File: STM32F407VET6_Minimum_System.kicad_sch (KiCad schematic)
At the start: 29 parts, among them J2 Conn_01x05, J4 Barrel_Jack, Q1 AO3401A, SW2 SW_DIP_x01, U1 STM32F407VET, U2 AMS1117-3.3, Y1 8MHz

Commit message: fix: adjust the wiring label
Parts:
- removed J2: Conn_01x05, symbol Connector_Generic:Conn_01x05
- renumbered C13 to C1, C8 to C10, C15 to C11, C9 to C12, C10 to C13, C16 to C14, C5 to C15, C11 to C16, C12 to C17, C20-bulk to C18, C14 to C2, C20 to C3, C1 to C4, C2 to C5, C19 to C6, C6 to C7, C4 to C8, C7 to C9, F2 to F1, J4 to J1, R6 to R2, SW2 to SW1
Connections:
- net +3.3V: now also C6.2, U1.6 (VBAT); no longer C6.1
- net GND: now also C6.1
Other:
- moved on the sheet: C6

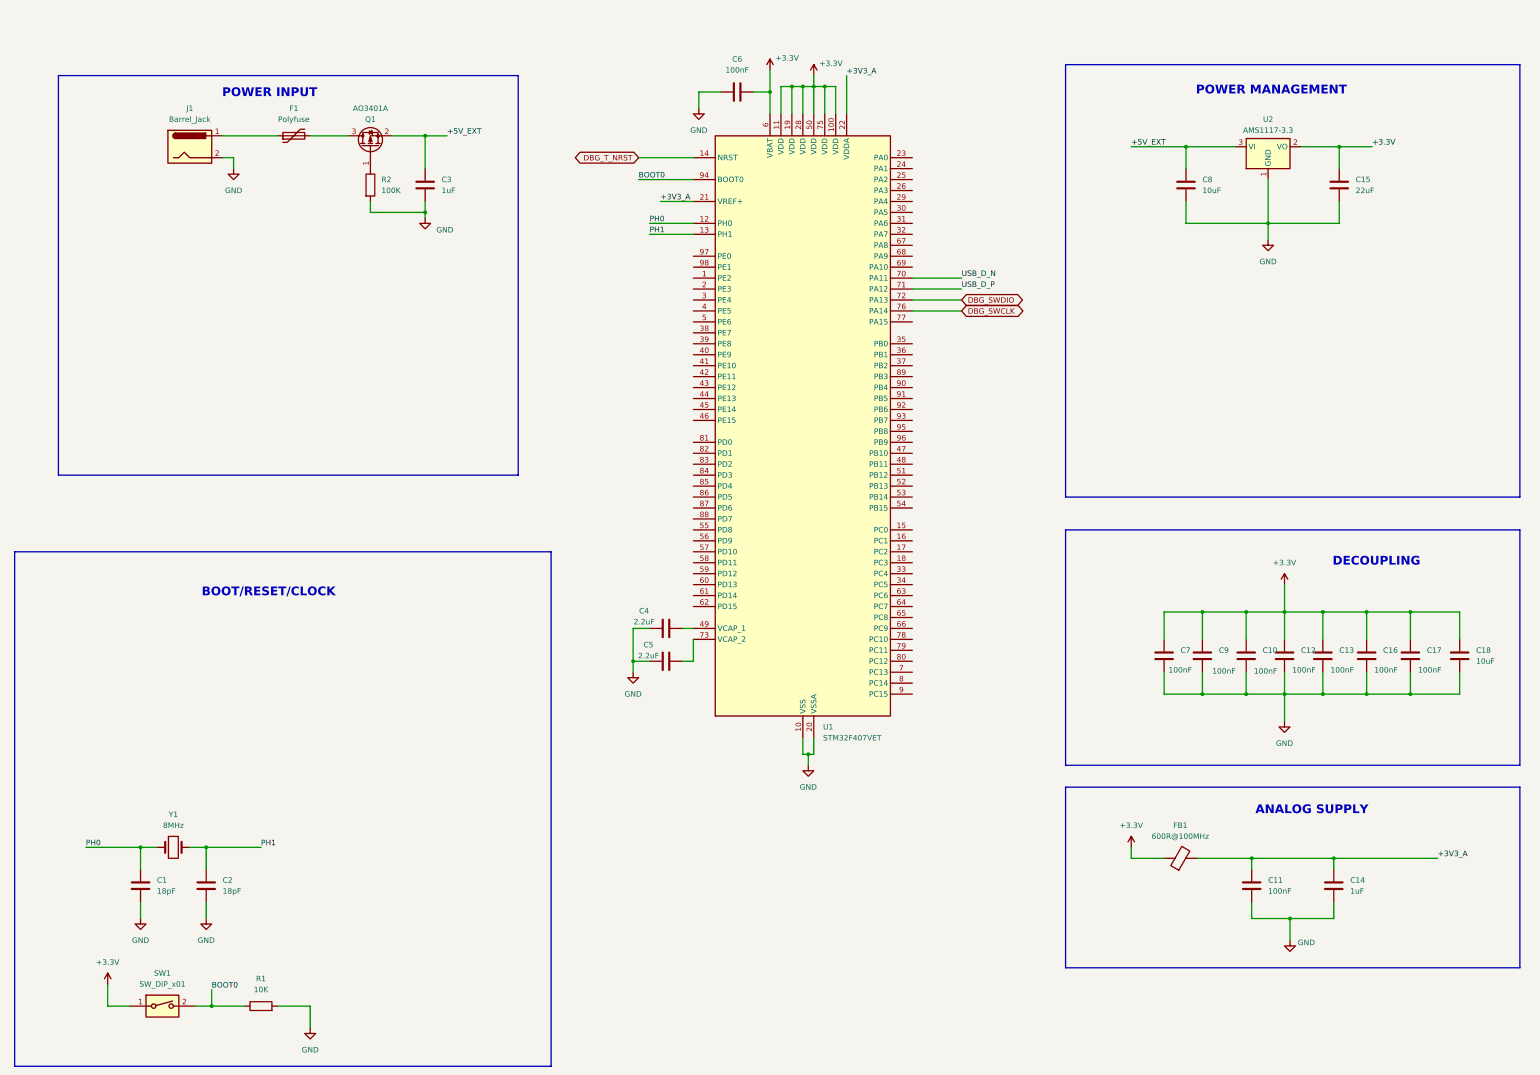
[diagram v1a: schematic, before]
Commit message: fix: revise power supply and onboard debug circuitry
Separate power sheet, add dual buck regulation and USB/DC isolation, and add debug isolation jumpers, programming headers and target reset. Include schematic PDF, ERC report and remaining validation requirements.
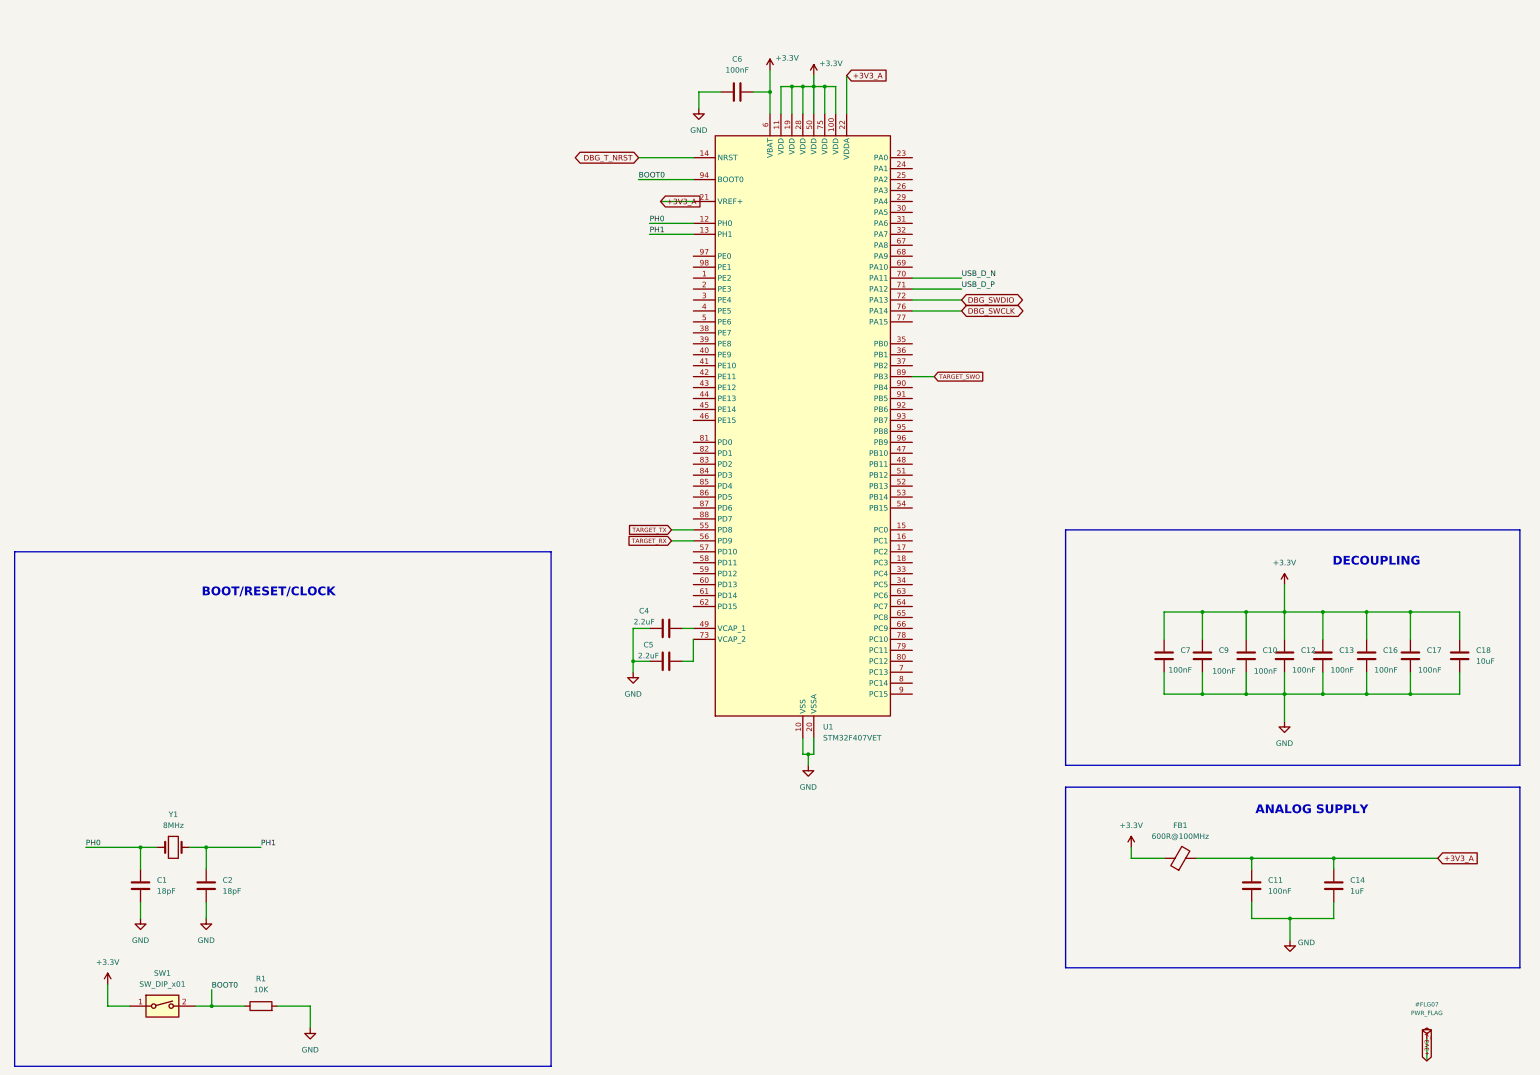
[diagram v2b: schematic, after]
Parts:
- removed C15: 22uF, symbol Device:C
- removed C3: 1uF, symbol Device:C
- removed C8: 10uF, symbol Device:C
- removed F1: Polyfuse, symbol Device:Polyfuse
- removed J1: Barrel_Jack, symbol Connector:Barrel_Jack
- removed Q1: AO3401A, Package_TO_SOT_SMD:SOT-23, symbol Transistor_FET:AO3401A
- removed R2: 100K, symbol Device:R
- removed U2: AMS1117-3.3, Package_TO_SOT_SMD:SOT-223-3_TabPin2, symbol Regulator_Linear:AMS1117-3.3
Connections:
- net TARGET_TX: now reaches U1.55 (PD8)
- net TARGET_RX: now reaches U1.56 (PD9)
- net TARGET_SWO: now reaches U1.89 (PB3)
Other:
- note removed: "POWER INPUT"
- note removed: "POWER MANAGEMENT"

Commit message: Revert "fix: revise power supply and onboard debug circuitry"
This reverts commit 2d890f2299649650f44a02df67d759df60ae0ebd.
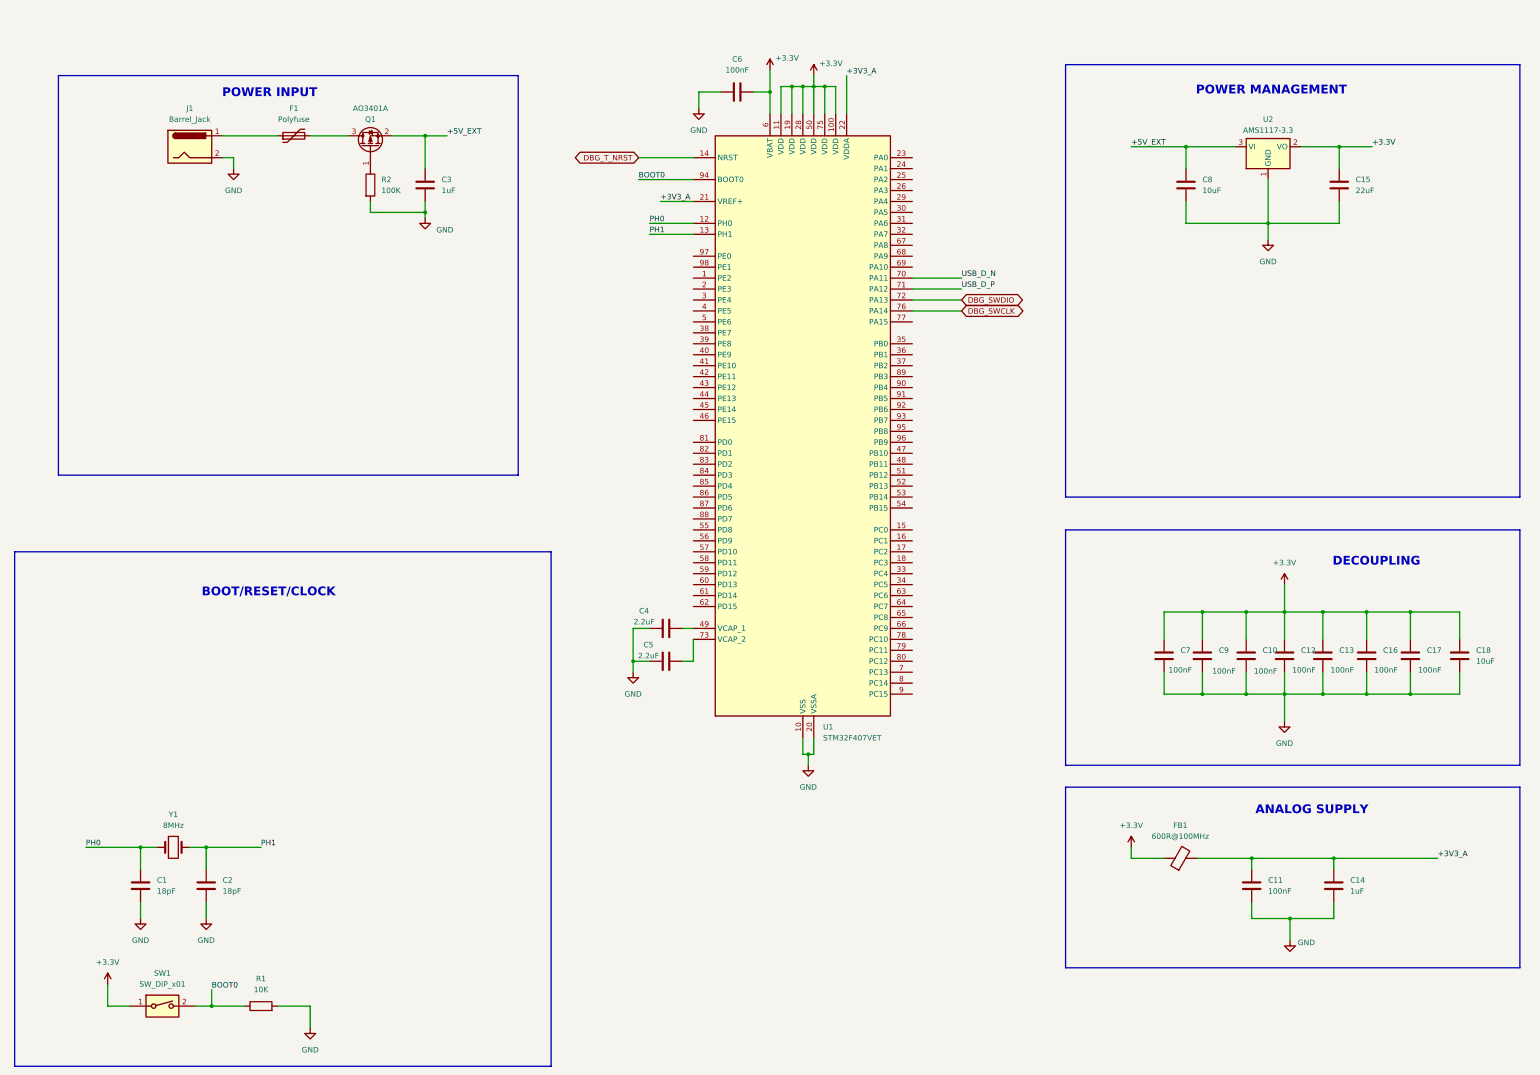
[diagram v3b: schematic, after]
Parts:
- added C15: 22uF, symbol Device:C
- added C3: 1uF, symbol Device:C
- added C8: 10uF, symbol Device:C
- added F1: Polyfuse, symbol Device:Polyfuse
- added J1: Barrel_Jack, symbol Connector:Barrel_Jack
- added Q1: AO3401A, Package_TO_SOT_SMD:SOT-23, symbol Transistor_FET:AO3401A
- added R2: 100K, symbol Device:R
- added U2: AMS1117-3.3, Package_TO_SOT_SMD:SOT-223-3_TabPin2, symbol Regulator_Linear:AMS1117-3.3
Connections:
- net +3.3V: now also C15.1, U2.2 (VO)
- net GND: now also C15.2, C3.2, C8.2, J1.2, R2.2, U2.1 (GND)
- net TARGET_RX: no longer names the net of U1.56 (PD9)
- net TARGET_SWO: no longer names the net of U1.89 (PB3)
- net TARGET_TX: no longer names the net of U1.55 (PD8)
- new net: F1.1, J1.1
- new net: F1.2, Q1.3 (D)
- new net: Q1.1 (G), R2.1
- new net +5V_EXT: C3.1, C8.1, Q1.2 (S), U2.3 (VI)
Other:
- note added: "POWER INPUT"
- note added: "POWER MANAGEMENT"

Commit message: refactor: add the new buck converter 12V
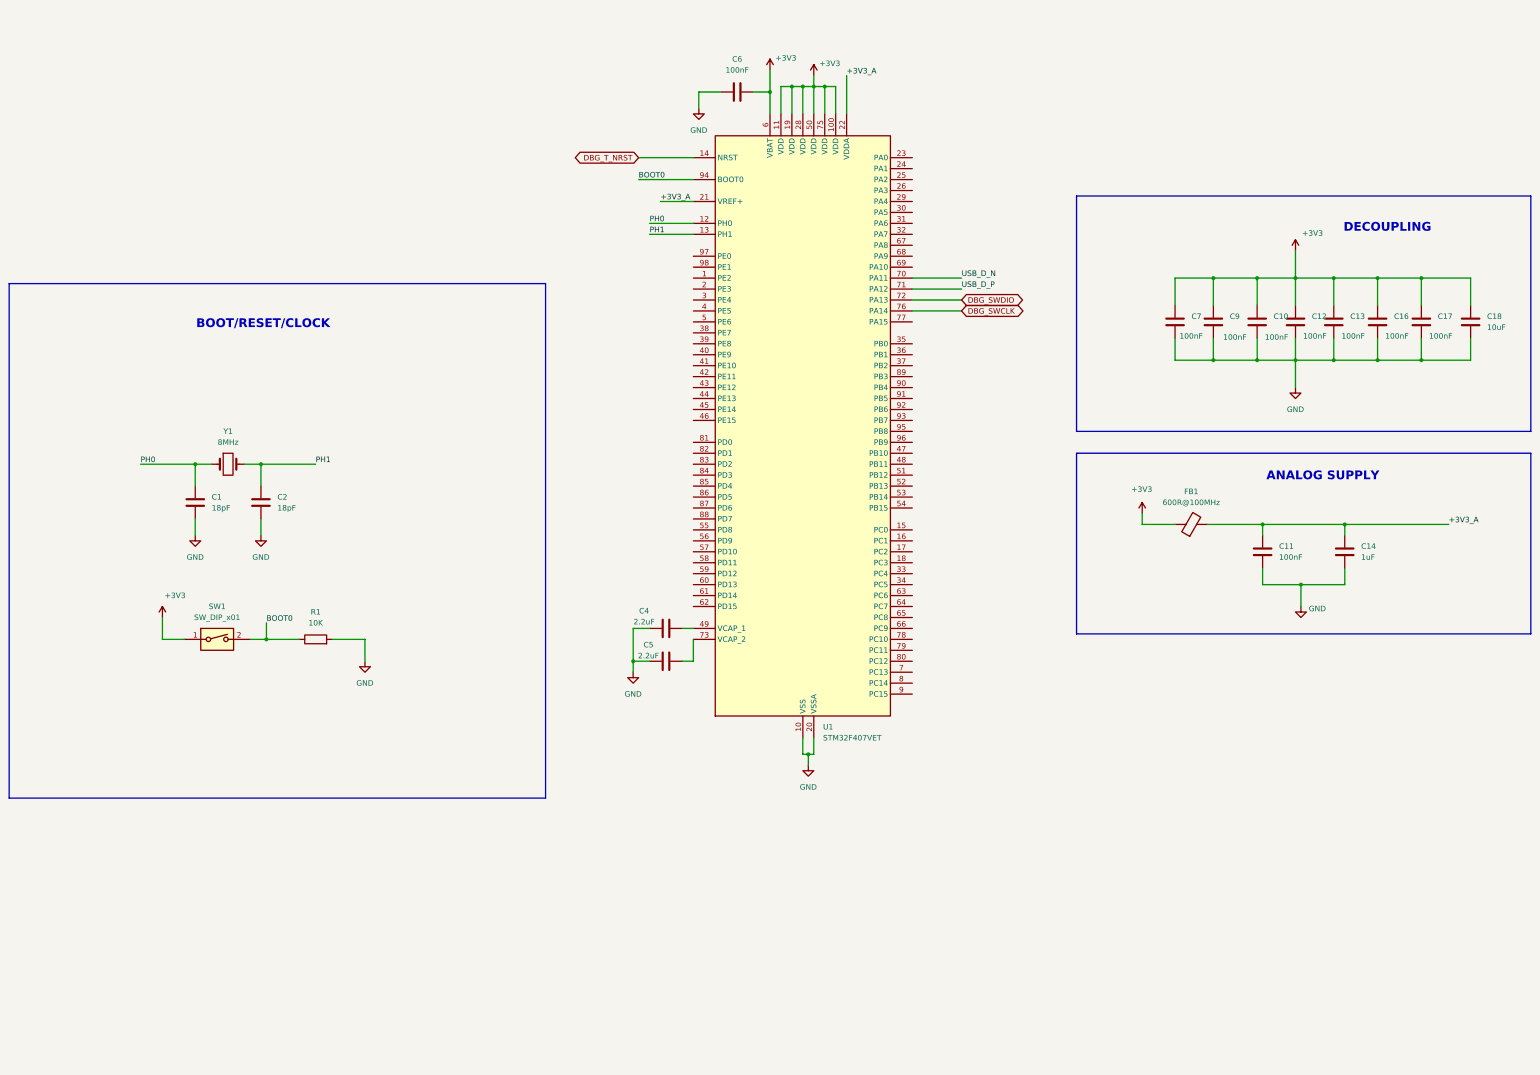
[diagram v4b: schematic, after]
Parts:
- removed C15: 22uF, symbol Device:C
- removed C3: 1uF, symbol Device:C
- removed C8: 10uF, symbol Device:C
- removed F1: Polyfuse, symbol Device:Polyfuse
- removed J1: Barrel_Jack, symbol Connector:Barrel_Jack
- removed Q1: AO3401A, Package_TO_SOT_SMD:SOT-23, symbol Transistor_FET:AO3401A
- removed R2: 100K, symbol Device:R
- removed U2: AMS1117-3.3, Package_TO_SOT_SMD:SOT-223-3_TabPin2, symbol Regulator_Linear:AMS1117-3.3
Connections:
- net +3.3V renamed +3V3
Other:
- note removed: "POWER INPUT"
- note removed: "POWER MANAGEMENT"
- moved on the sheet: C1, C10, C11, C12, C13, C14, C16, C17, C18, C2, C7, C9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

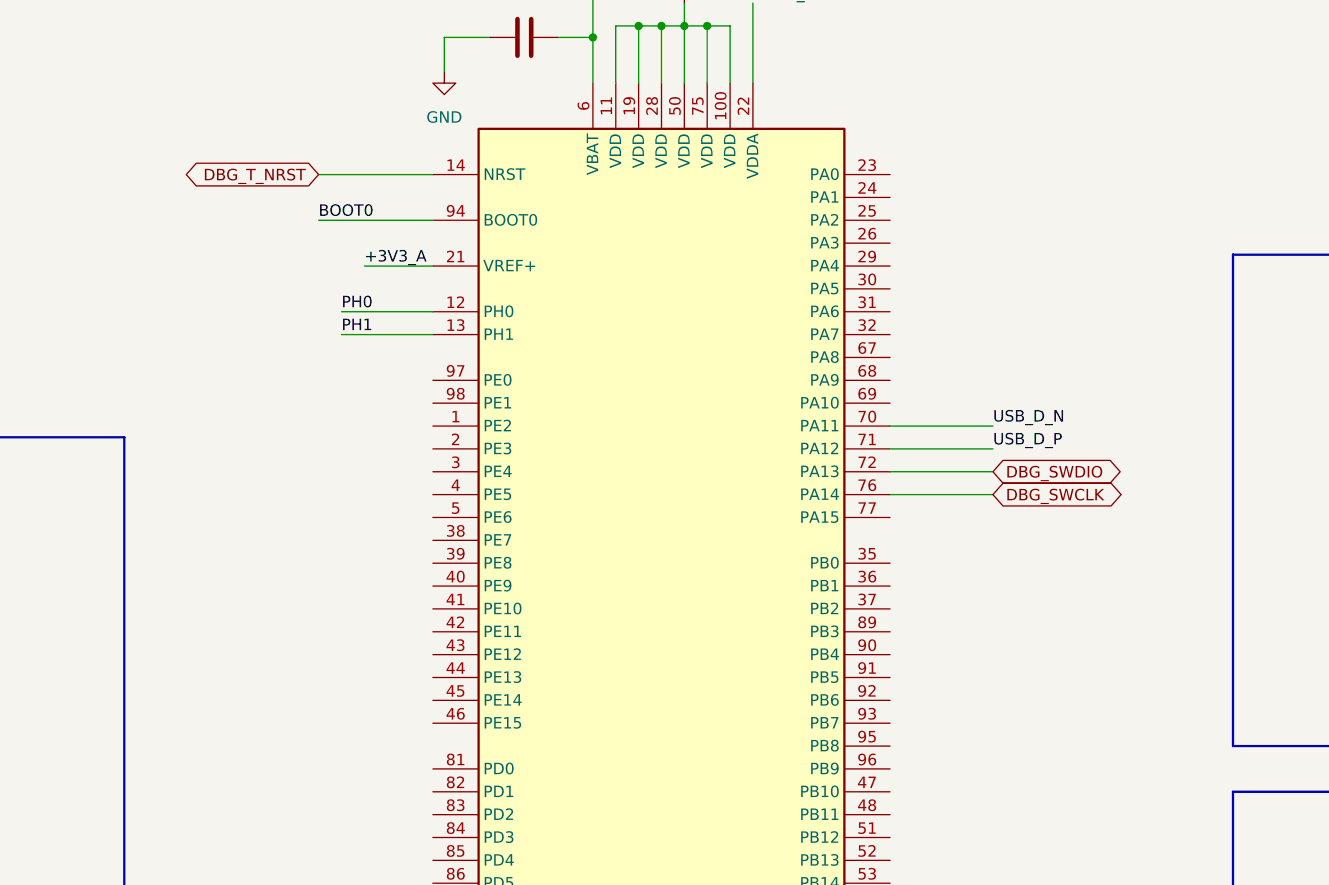
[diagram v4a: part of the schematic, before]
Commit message: feat: add the basic io schematic
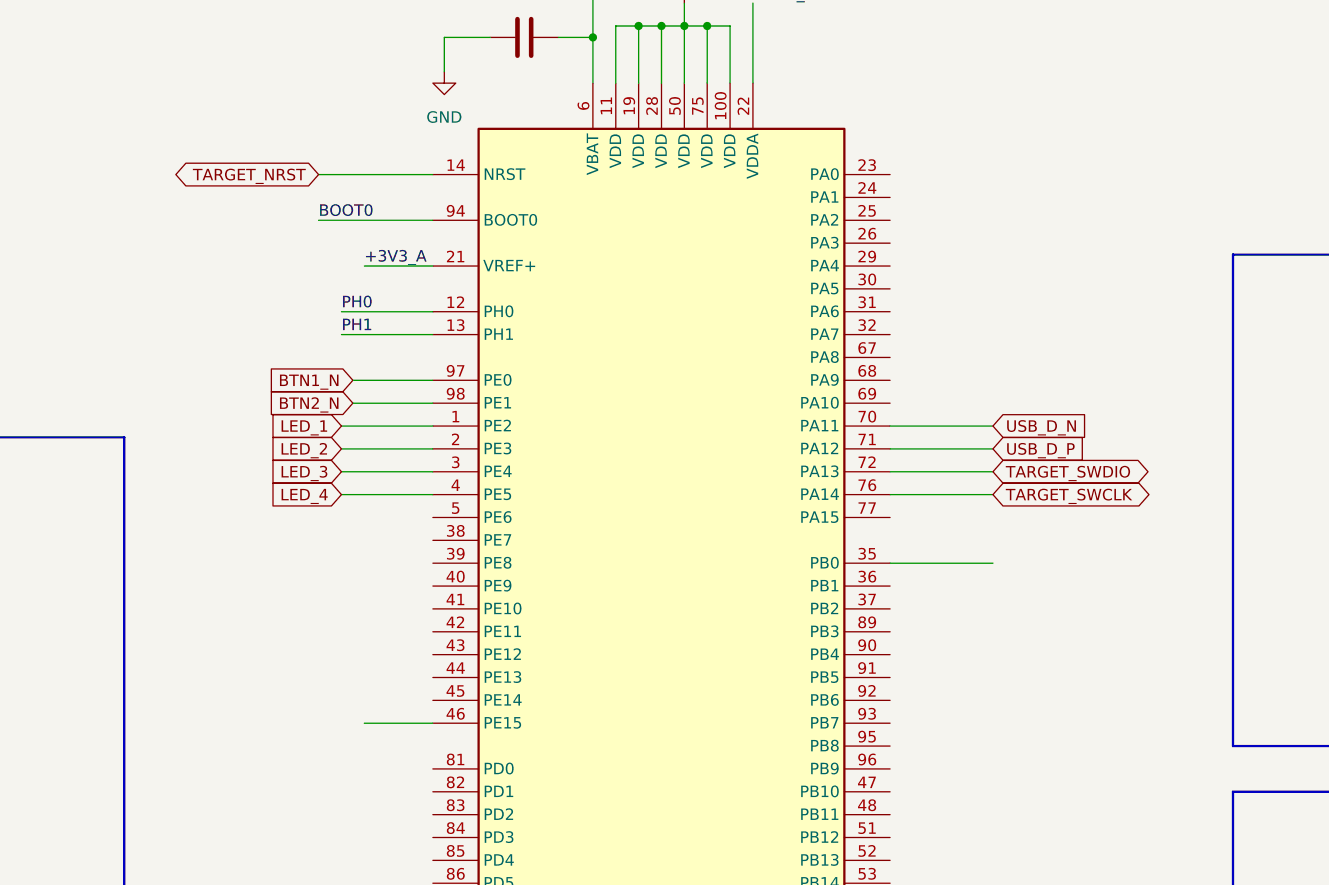
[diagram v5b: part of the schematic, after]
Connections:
- net LED_1: now reaches U1.1 (PE2)
- net LED_2: now reaches U1.2 (PE3)
- net LED_3: now reaches U1.3 (PE4)
- net LED_4: now reaches U1.4 (PE5)
- net BTN1_N: now reaches U1.97 (PE0)
- net BTN2_N: now reaches U1.98 (PE1)
- net DBG_SWCLK renamed TARGET_SWCLK
- net DBG_SWDIO renamed TARGET_SWDIO
- net DBG_T_NRST renamed TARGET_NRST
